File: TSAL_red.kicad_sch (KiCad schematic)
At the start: 5 parts, among them U4 ADUM5202WCRWZ

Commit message: Saved. Initial Structure done.
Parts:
- added R1: 1k, symbol Device:R
- C1, C4: value C_Small -> 100nF
- C2, C3: value C_Small -> 10uF
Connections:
- net at C3.1, C4.1, U4.16 (VISO): now also U4.11 (VSEL)
- net at C3.2, C4.2, U4.15 (GNDISO): now also U4.9 (GNDISO)
- net at U4.13 (VIB): now also R1.1
- new net HV_RED-: R1.2
- no-connect marks 0 -> 1
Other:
- moved on the sheet: C3, C4

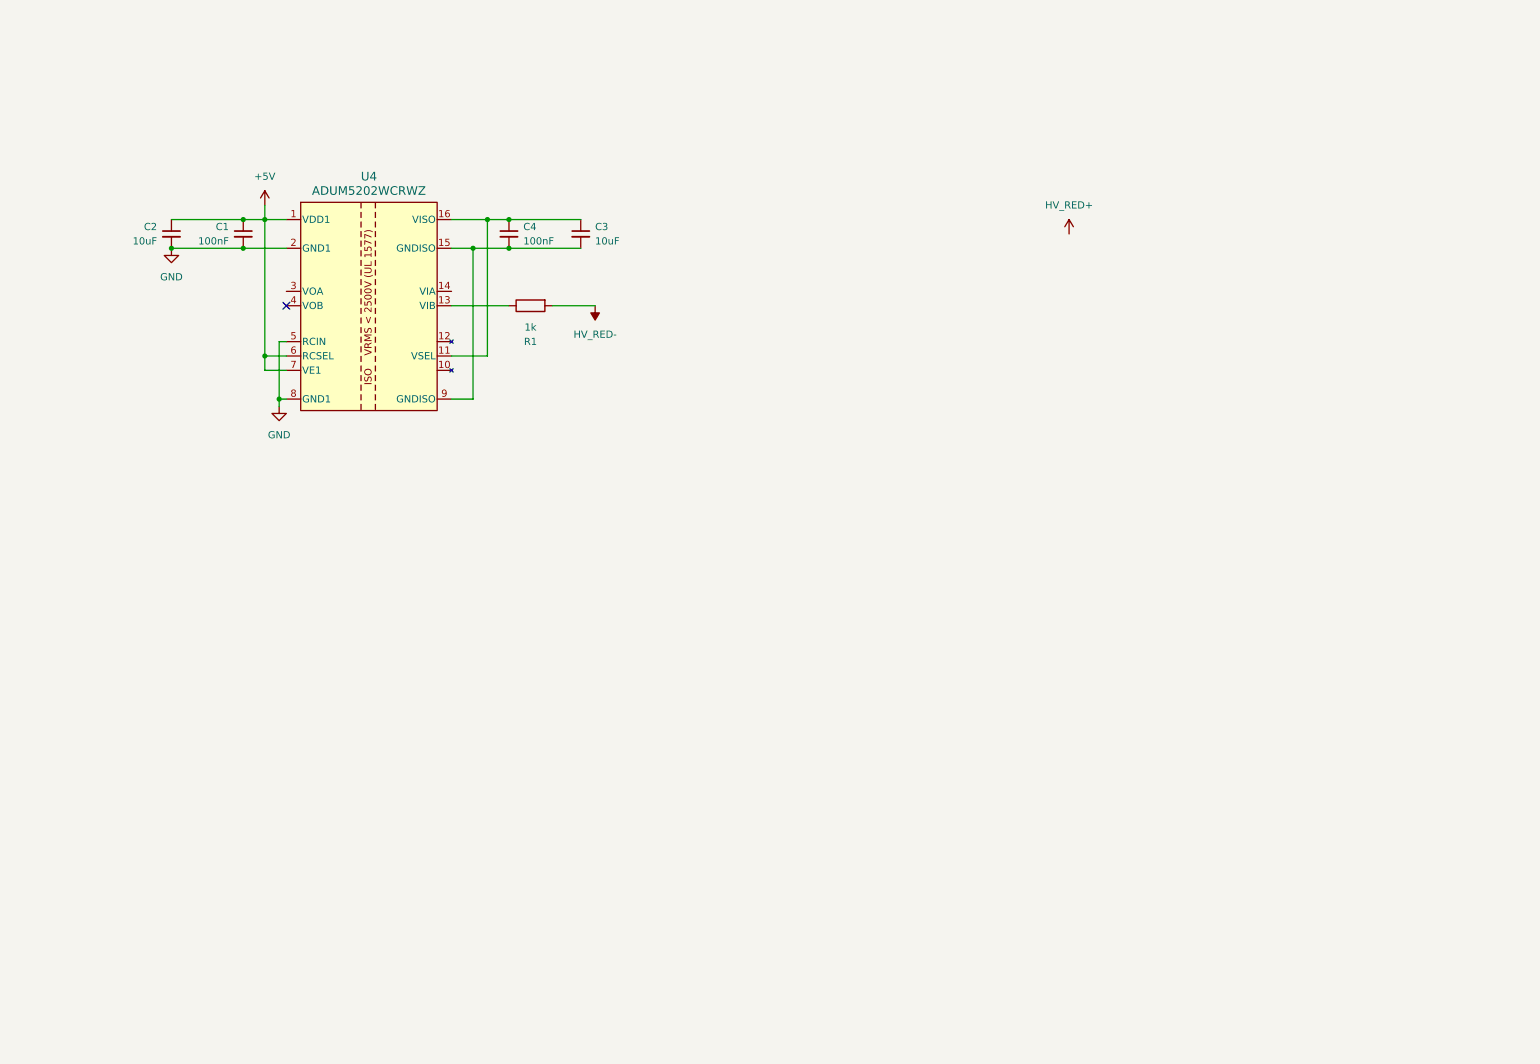
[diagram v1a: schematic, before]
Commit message: added OPA and HV Resistors
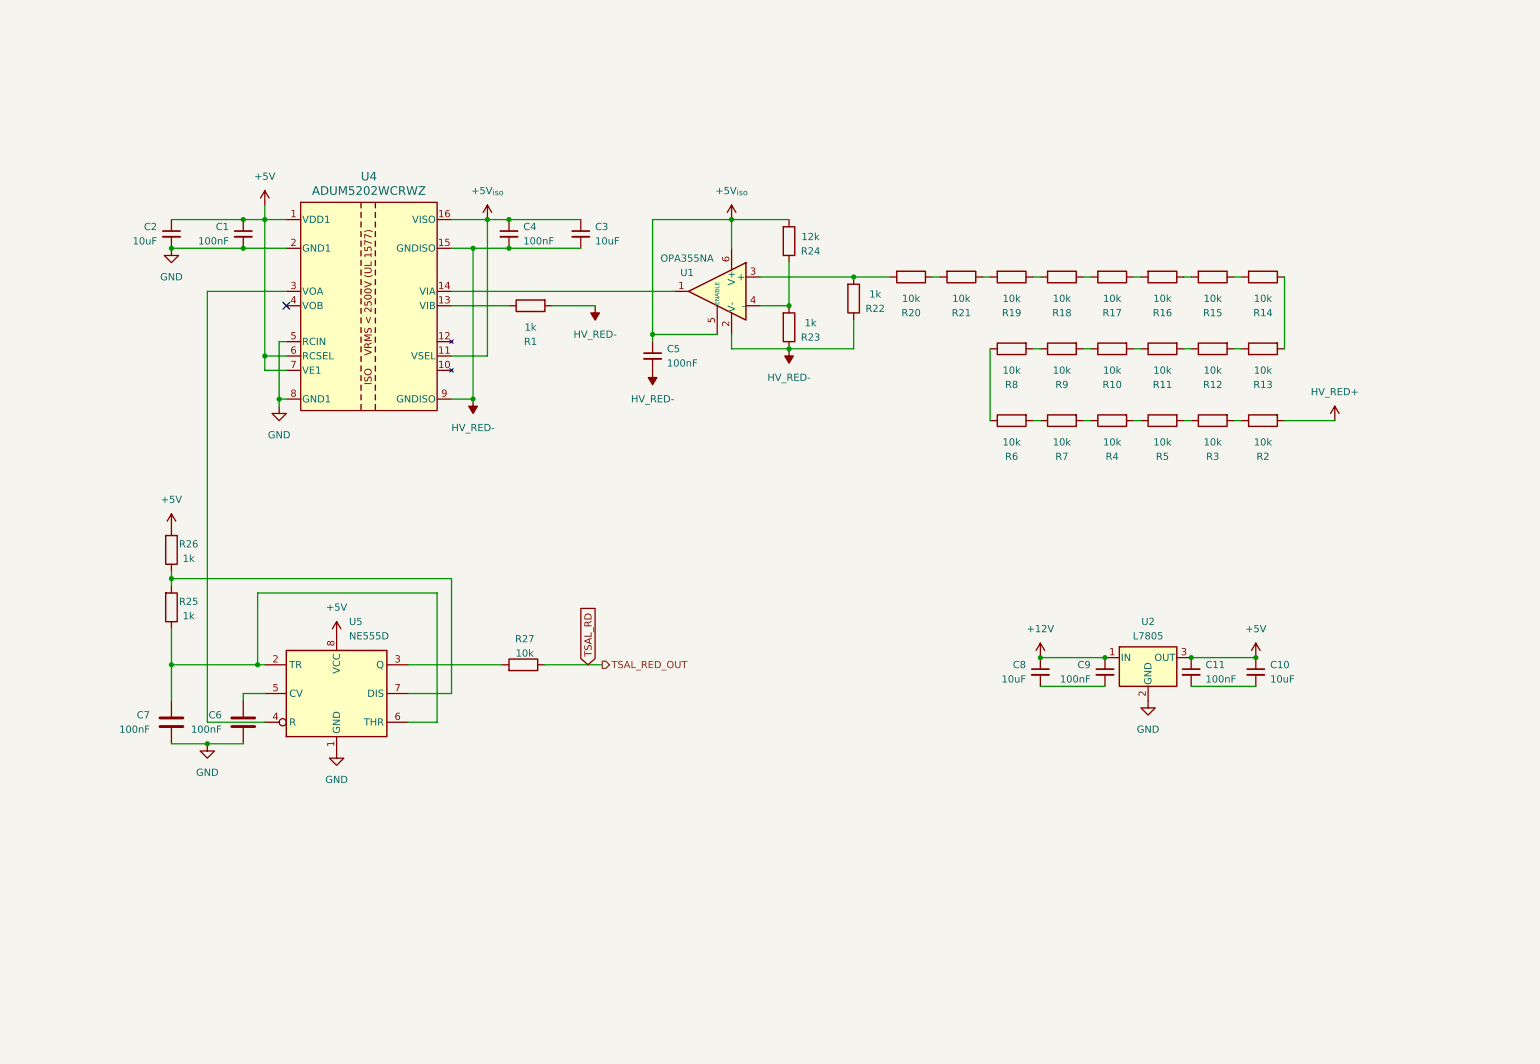
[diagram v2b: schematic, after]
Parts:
- added C10, C8: 10uF, symbol Device:C_Small
- added C11, C5, C9: 100nF, symbol Device:C_Small
- added C6, C7: 100nF, symbol Device:C
- added R10, R11, R12, R13, R14, R15, R16, R17, R18, R19, R2, R20, R21, R27, R3, R4, R5, R6, R7, R8, R9: 10k, symbol Device:R
- added R22, R23, R25, R26: 1k, symbol Device:R
- added R24: 12k, symbol Device:R
- added U1: OPA355NA, Package_TO_SOT_SMD:SOT-23-6, symbol Amplifier_Operational:OPA355NA
- added U2: L7805, symbol Regulator_Linear:L7805
- added U5: NE555D, Package_SO:SOIC-8_3.9x4.9mm_P1.27mm, symbol Timer:NE555D
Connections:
- net  HV_RED+: now also R2.2
- net +5V: now also C10.1, C11.1, R26.2, U2.3 (OUT), U5.8 (VCC)
- net GND: now also C6.2, C7.2, U2.2 (GND), U5.1 (GND)
- net HV_RED-: now also C3.2, C4.2, U4.15 (GNDISO), U4.9 (GNDISO), C5.2, R22.1, R23.1, U1.2 (V-)
- net +5V_{iso}: now reaches C3.1, C4.1, U4.11 (VSEL), U4.16 (VISO)
- net +5V_{iso}: now also C5.1, R24.2, U1.5 (ENABLE), U1.6 (V+)
- net at U4.14 (VIA): now also U1.1
- net at U4.3 (VOA): now also U5.4 (R)
- new net: R25.2, R26.1, U5.7 (DIS)
- new net: R23.2, R24.1, U1.4 (-)
- new net: C10.2, C11.2
- new net: R20.2, R22.2, U1.3 (+)
- new net: R10.2, R11.1
- new net: R11.2, R12.1
- new net: C8.2, C9.2
- new net: R16.2, R17.1
- new net: R17.2, R18.1
- new net: R8.2, R9.1
- new net: R10.1, R9.2
- new net: R4.1, R7.2
- new net: R4.2, R5.1
- new net: R18.2, R19.1
- new net: R12.2, R13.1
- new net: R13.2, R14.1
- new net: R14.2, R15.1
- new net: R15.2, R16.1
- new net: R3.1, R5.2
- new net: R2.1, R3.2
- new net: C7.1, R25.1, U5.2 (TR), U5.6 (THR)
- new net: R27.2, U5.3 (Q)
- new net: C6.1, U5.5 (CV)
- new net: R20.1, R21.2
- new net: R19.2, R21.1
- new net: R6.2, R7.1
- new net: R6.1, R8.1
- new net +12V: C8.1, C9.1, U2.1 (IN)
- new net TSAL_RD: R27.1

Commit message: Added *.lck to gitignore
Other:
- note added: "CHECK ACTIVATION CIRCUIT"
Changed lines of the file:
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@@
+		)
+	)
+	(text "CHECK ACTIVATION CIRCUIT"
+		(exclude_from_sim no)
+		(at 139.7 64.262 0)
+		(effects
+			(font
+				(size 3 3)
+				(thickness 0.6)
+				(bold yes)
+				(color 255 0 32 1)
+			)
 		)
 	)

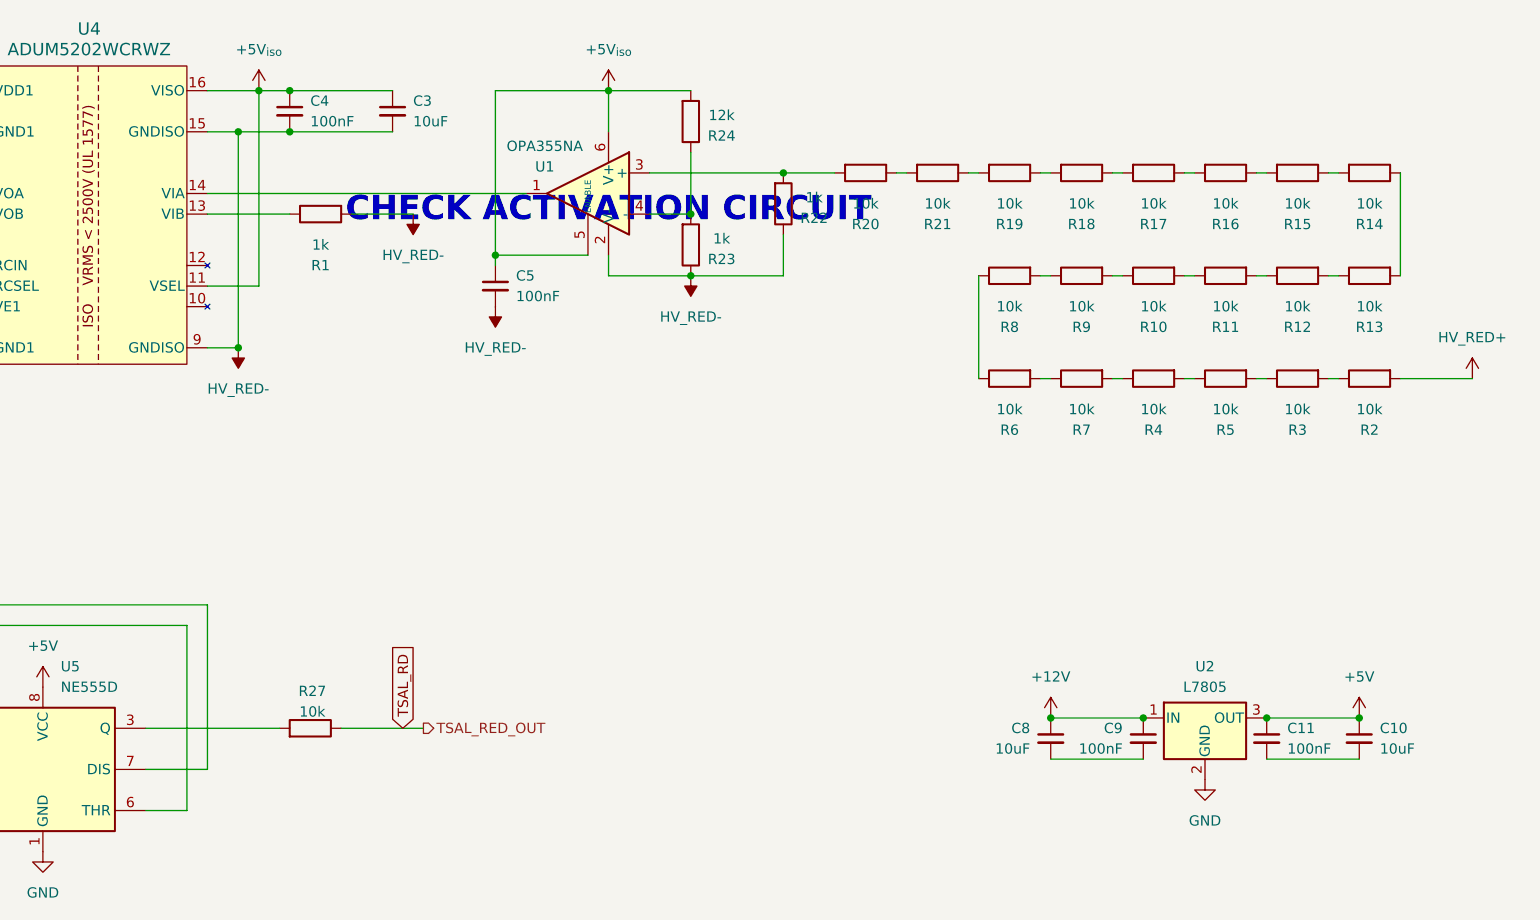
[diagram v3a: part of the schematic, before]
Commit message: Changes to Pinout pending
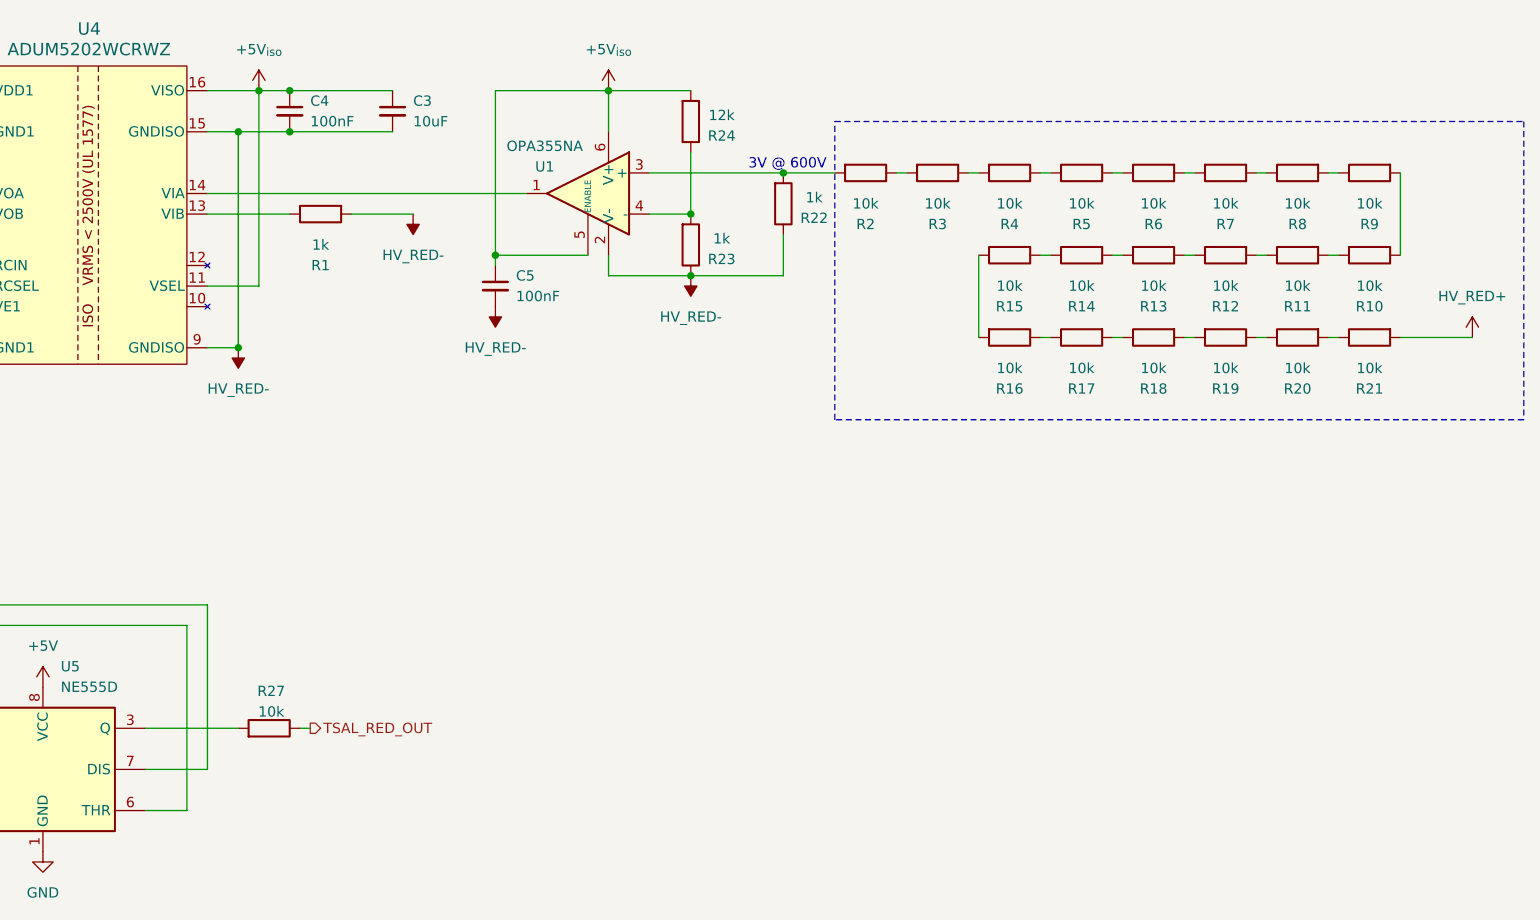
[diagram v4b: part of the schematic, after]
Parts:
- removed C10, C8: 10uF, symbol Device:C_Small
- removed C11, C9: 100nF, symbol Device:C_Small
- removed U2: L7805, symbol Regulator_Linear:L7805
- C1, C2, C3, C4, C5, C6, C7: footprint (none) -> Capacitor_SMD:C_0603_1608Metric
- R1, R10, R11, R12, R13, R14, R15, R16, R17, R18, R19, R2, R20, R21, R22, R23, R24, R25, R26, R27, R3, R4, R5, R6, R7, R8, R9: footprint (none) -> Resistor_SMD:R_0603_1608Metric
- U1: Cost (none) -> 1,62; Mouser (none) -> 595-OPA355NA/3K
- U4: Cost (none) -> 12,90; Mouser (none) -> 584-ADUM5202WCRWZ
- U5: Cost (none) -> 0,40; Mouser (none) -> 595-NE555DR
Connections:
- net  HV_RED+: now also R21.2; no longer R2.2
- net at R22.2, U1.3 (+): now also R2.2; no longer R20.2
- net at R11.1: now also R12.2; no longer R10.2
- net at R11.2: now also R10.2; no longer R12.1
- net at R17.1: now also R16.1; no longer R16.2
- net at R4.1: now also R5.1; no longer R7.2
- net at R4.2: now also R3.1; no longer R5.1
- net at R18.2: now also R19.2; no longer R19.1
- net at R13.1: now also R12.1; no longer R12.2
- net at R14.1: now also R15.2; no longer R13.2
- net at R14.2: now also R13.2; no longer R15.1
- net at R5.2: now also R6.1; no longer R3.1
- net at R20.1: now also R19.1; no longer R21.2
- net at R21.1: now also R20.2; no longer R19.2
- net at R7.1: now also R8.1; no longer R6.2
- net TSAL_RD renamed TSAL_RED_OUT
- new net: R6.2, R7.2
- new net: R15.1, R16.2
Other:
- note added: "3V @ 600V"
- note removed: "CHECK ACTIVATION CIRCUIT"
- moved on the sheet: R27

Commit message: Changed Layout
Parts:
- removed C1, C4: 100nF, Capacitor_SMD:C_0603_1608Metric, symbol Device:C_Small
- removed C2, C3: 10uF, Capacitor_SMD:C_0603_1608Metric, symbol Device:C_Small
- removed U4: ADUM5202WCRWZ, RW_16_ADI, symbol ADUM5202:ADUM5202WCRWZ
- added R67: 1k, Resistor_SMD:R_0603_1608Metric, symbol Device:R
- added U17: TBA1-0511E, Converter_DCDC:Converter_DCDC_TRACO_TBA1-xxxxE_Single_THT, symbol Converter_DCDC:TBA1-0511E
- added U4: SFH617A-1X007T, Package_DIP:SMDIP-4_W9.53mm_Clearance8mm, symbol Isolator:SFH617A-1X007T
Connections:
- net +5V: now also U17.1 (+Vin), U4.4
- net GND: now also R1.1, U17.2 (-Vin)
- net at U1.1: now also U4.1
- net at U5.4 (R): now also R1.2, U4.3
- net  HV_RED+ renamed TS+
- net +5V_{iso} renamed +5V_{iso_RED}
- net +5V_{iso_RED}: now also U17.6 (+Vout)
- net HV_RED- renamed TS-
- net TS-: now also R67.1, U17.4 (-Vout); no longer R1.2
- new net: R67.2, U4.2
- no-connect marks 1 -> 0
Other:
- note added: "ISO 1.5kV"
- note added: "ISO 3750kV_{rms}"
- moved on the sheet: C5, C6, C7, R10, R11, R12, R13, R14, R15, R16, R17, R18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
